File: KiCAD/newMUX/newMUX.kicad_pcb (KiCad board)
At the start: 4 copper layers, 40 x 89 mm, 43 parts, among them J1 Conn_01x14, J2 Conn_02x06_Odd_Even, J3 Conn_02x06_Odd_Even, J4 Conn_01x14, U1 ASSR-1611, U10 ASSR-1611, U11 ASSR-1611, U12 ASSR-1611, U13 ASSR-1611, U14 ASSR-1611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

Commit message: update silk
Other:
- board text added: "c75b306"
- board text removed: "1ad7c5f"
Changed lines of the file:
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@@
   )
   (setup
-    (last_trace_width 1)
+    (last_trace_width 0.25)
     (user_trace_width 0.43)
     (user_trace_width 1)
@@
   (gr_arc (start -17.5 -42) (end -17.5 -44.5) (angle -90) (layer Edge.Cuts) (width 0.15))
   (gr_arc (start 17.5 -42) (end 20 -42) (angle -90) (layer Edge.Cuts) (width 0.15))
-  (gr_text 1ad7c5f (at -18.796 -21.844 90) (layer F.SilkS)
+  (gr_text c75b306 (at -18.796 -21.844 90) (layer F.SilkS)
     (effects (font (size 1 1) (thickness 0.25)))
   )

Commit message: wip commit
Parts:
- RN1, RN2, RN3, RN4, RN5: footprint Resistors_SMD:R_Cat16-4 -> myParts:VISHAY_CRA12E
- moved RN1 0.61 mm to (2.50, 23.0)
- moved RN2 0.61 mm to (-2.50, 23.0)
- moved RN4 0.60 mm to (-2.50, -11.5)
- moved RN5 0.60 mm to (2.50, -11.5)
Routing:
- net Net-(RN1-Pad4): track 22.8 -> 2.97 mm, vias 1 -> 0
- net GND: track 207.1 -> 201.3 mm
- net Net-(RN3-Pad4): track 55.2 -> 59.9 mm, vias 1 -> 2
- net /P7: track 79.7 -> 76.9 mm
- net Net-(RN5-Pad6): track 17.4 -> 20.0 mm
- net Net-(RN5-Pad5): track 43.6 -> 45.7 mm, vias 1 -> 0
- net Net-(RN2-Pad7): track 18.3 -> 20.2 mm, vias 1 -> 2
- net Net-(RN4-Pad2): track 25.6 -> 23.8 mm
- net Net-(R1-Pad2): track 42.6 -> 44.4 mm, vias 3 -> 4
- net Net-(RN2-Pad6): track 10.7 -> 12.3 mm
- net Net-(RN2-Pad5): track 12.2 -> 10.6 mm
- net Net-(RN5-Pad7): track 4.05 -> 2.46 mm, vias 1 -> 0
- net Net-(RN3-Pad1): track 33.3 -> 34.9 mm, vias 1 -> 2
- net Net-(RN5-Pad8): track 12.6 -> 11.1 mm
- net Net-(RN1-Pad3): track 24.4 -> 25.9 mm
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
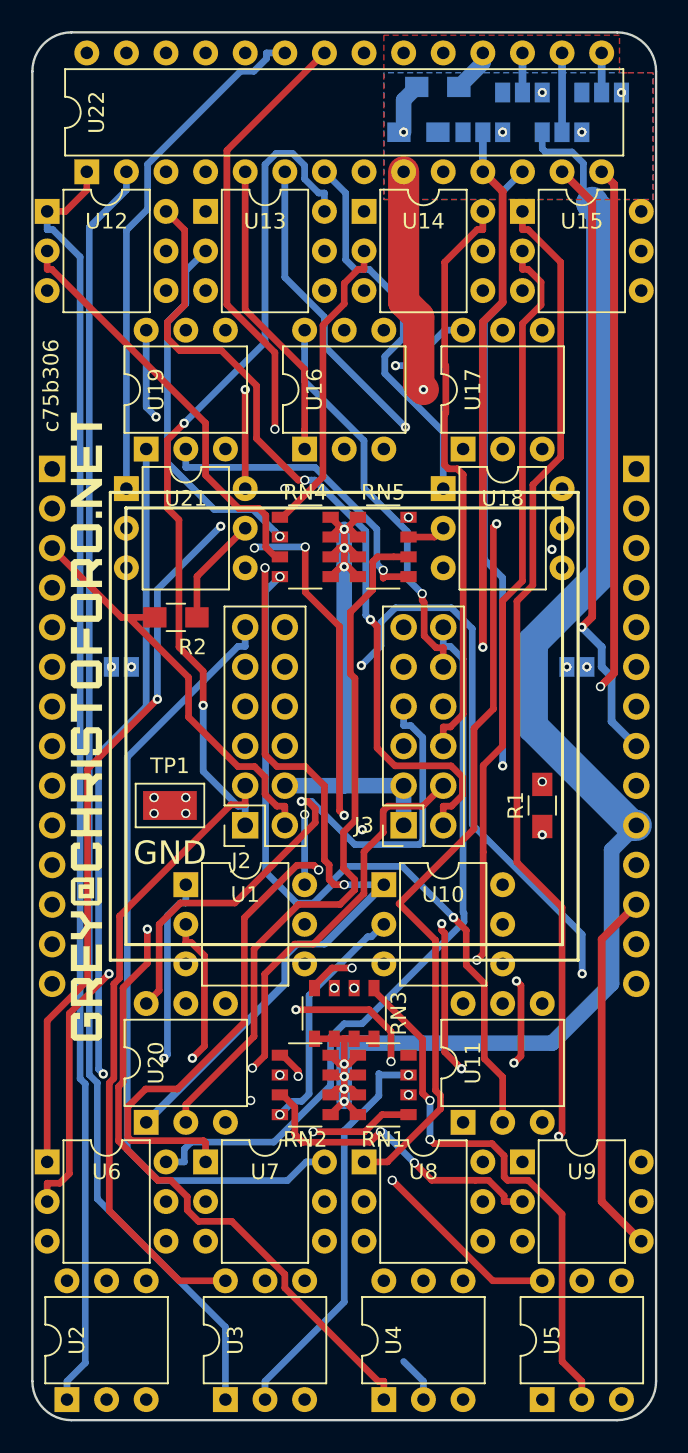
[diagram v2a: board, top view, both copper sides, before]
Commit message: rotate connectors on newMux
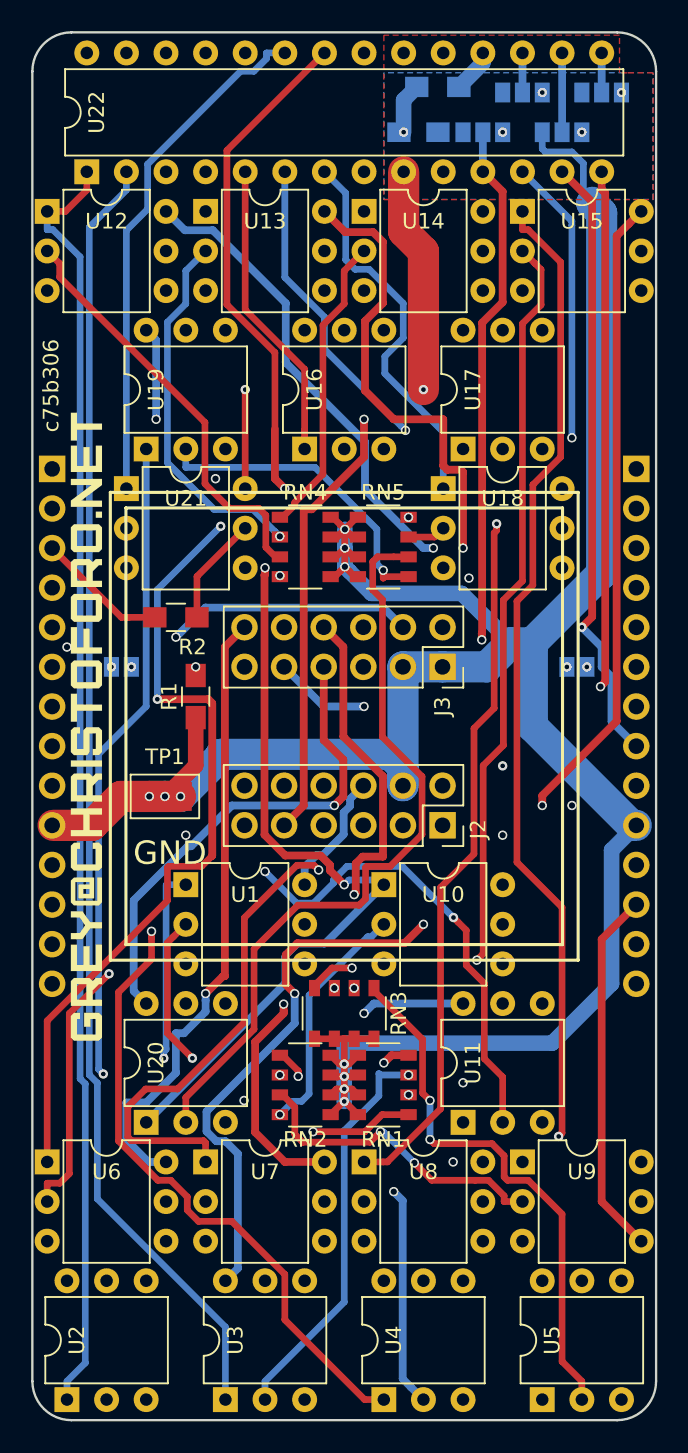
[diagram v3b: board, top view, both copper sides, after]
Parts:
- moved R1 23.3 mm to (-9.53, -1.91)
- moved J2 12.7 mm to (6.30, 6.35), turned to 270 degrees
- moved J3 10.5 mm to (6.30, -3.81), turned to 270 degrees
- moved TP1 0.66 mm to (-11.5, 4.50)
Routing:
- net Net-(R1-Pad2): track 44.4 -> 10.7 mm, vias 4 -> 1
- net /V6: track 50.9 -> 26.7 mm, vias 0 -> 1
- net /I4: track 75.9 -> 52.7 mm, vias 0 -> 1
- net GND: track 201.3 -> 178.2 mm, vias 12 -> 10
- net /I7: track 14.5 -> 36.4 mm, vias 0 -> 1
- net Net-(RN1-Pad4): track 2.97 -> 24.4 mm, vias 0 -> 2
- net /V1: track 45.0 -> 64.4 mm, vias 1 -> 2
- net /I1: track 53.3 -> 35.9 mm, vias 2 -> 1
- net I+: track 151.6 -> 135.0 mm
- net /V8: track 53.7 -> 44.7 mm, vias 2 -> 1
- net /I8: track 23.5 -> 31.8 mm
- net /V4: track 50.7 -> 42.7 mm, vias 3 -> 1
- net /V3: track 43.1 -> 50.5 mm, vias 2 -> 3
- net /I6: track 29.9 -> 37.2 mm
- net /V5: track 47.5 -> 40.3 mm, vias 0 -> 1
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
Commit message: update silk
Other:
- board text added: "3ec2e93"
- board text removed: "c75b306"
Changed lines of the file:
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@@
   )
   (setup
-    (last_trace_width 0.5)
+    (last_trace_width 0.25)
     (user_trace_width 0.43)
     (user_trace_width 0.5)
@@
     )
   )
+  (gr_text 3ec2e93 (at -18.415 -22.225 90) (layer F.SilkS)
+    (effects (font (size 1.5 1.5) (thickness 0.3)))
+  )
   (gr_text "GND\n" (at -11.176 8.128) (layer F.SilkS)
     (effects (font (size 1.5 1.5) (thickness 0.3)))
@@
   (gr_arc (start -17.5 -42) (end -17.5 -44.5) (angle -90) (layer Edge.Cuts) (width 0.15))
   (gr_arc (start 17.5 -42) (end 20 -42) (angle -90) (layer Edge.Cuts) (width 0.15))
-  (gr_text c75b306 (at -18.796 -21.844 90) (layer F.SilkS)
-    (effects (font (size 1 1) (thickness 0.25)))
-  )
   (gr_line (start 20 42) (end 20 -42) (layer Edge.Cuts) (width 0.15))
   (gr_line (start -20 42) (end -20 -42) (layer Edge.Cuts) (width 0.15))

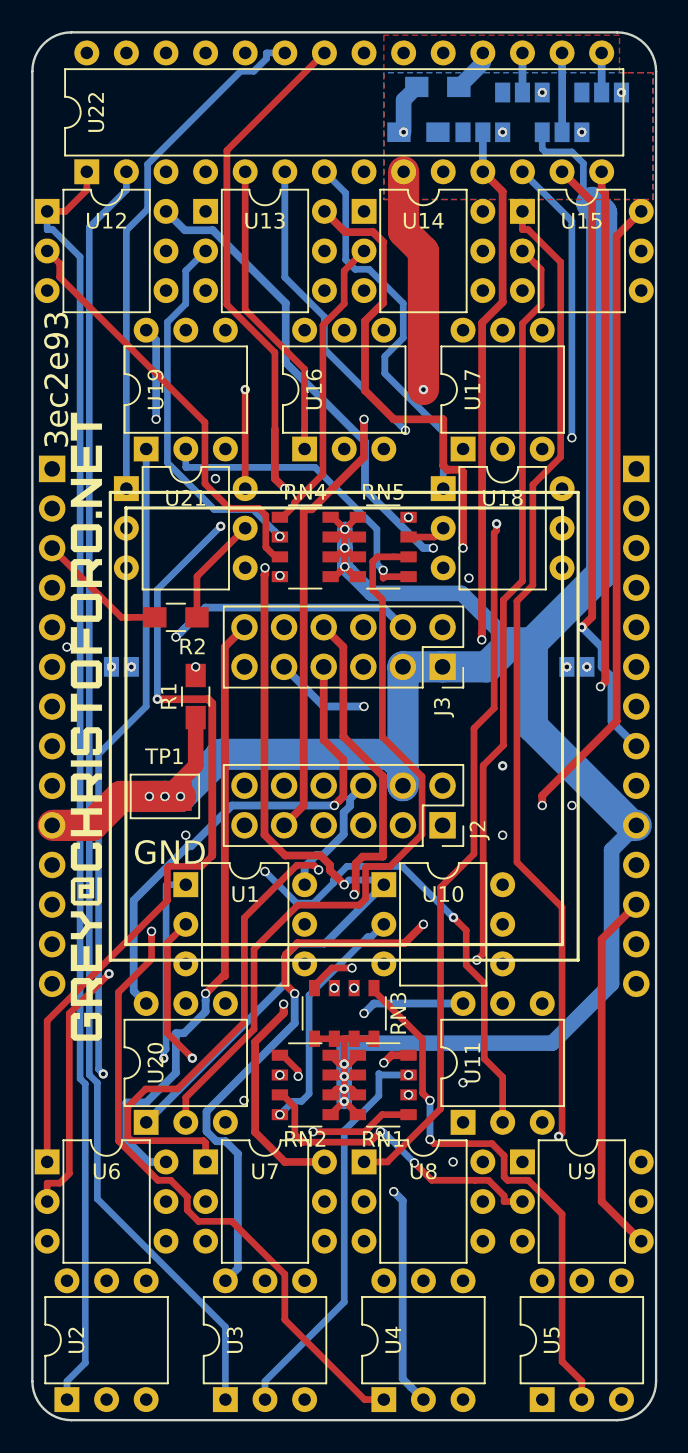
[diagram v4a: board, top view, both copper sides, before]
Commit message: starting on ethercat board pin boards rotated base1x zones fixed
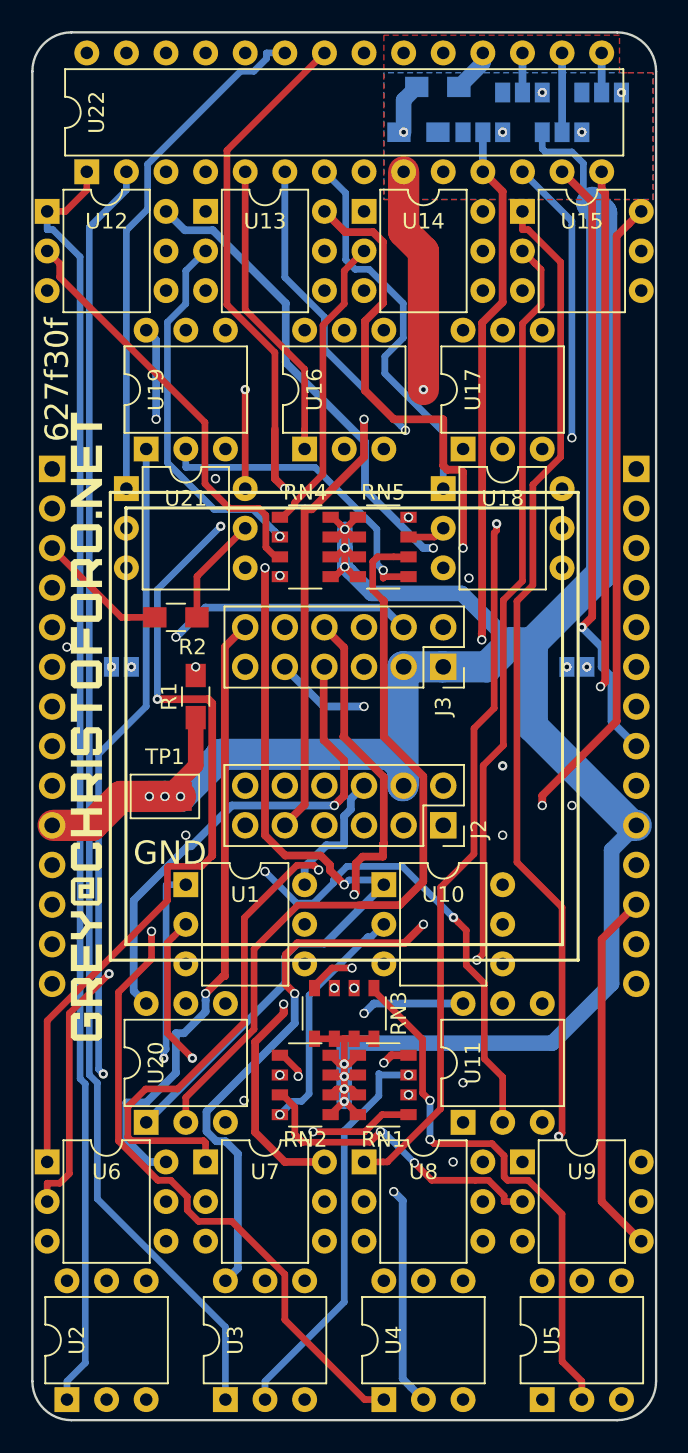
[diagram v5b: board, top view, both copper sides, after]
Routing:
- net Net-(RN5-Pad5): track 49.2 -> 49.9 mm
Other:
- board text added: "627f30f"
- board text removed: "3ec2e93"

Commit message: update silk
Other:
- board text added: "20b2bb8"
- board text removed: "627f30f"
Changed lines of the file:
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@@
-(kicad_pcb (version 20171130) (host pcbnew "(5.0-dev-4085-g9241a399a)")
+(kicad_pcb (version 20171130) (host pcbnew "(5.0.0-rc2-dev-44-gde6b32d23)")
   (general
     (thickness 1.6)
@@
   )
   (setup
-    (last_trace_width 0.5)
+    (last_trace_width 0.25)
     (user_trace_width 0.43)
     (user_trace_width 0.5)
@@
       (usegerberattributes true)
       (usegerberadvancedattributes true)
-      (creategerberjobfile true)
+      (creategerberjobfile false)
       (excludeedgelayer true)
       (linewidth 0.150000)
@@
     )
   )
-  (gr_text 627f30f (at -18.415 -22.225 90) (layer F.SilkS)
+  (gr_text 20b2bb8 (at -18.415 -22.225 90) (layer F.SilkS)
     (effects (font (size 1.5 1.5) (thickness 0.3)))
   )

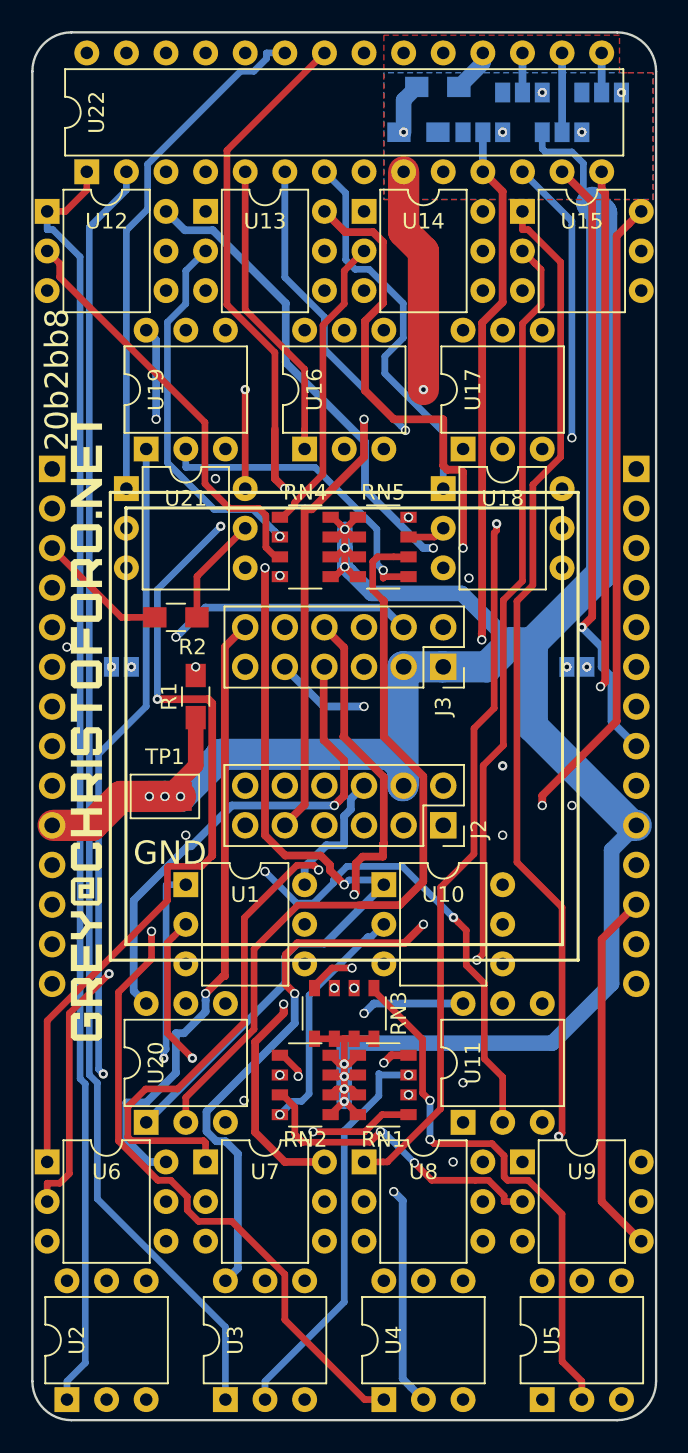
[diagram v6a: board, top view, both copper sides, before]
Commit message: upgrade syms and layouts to kicad5
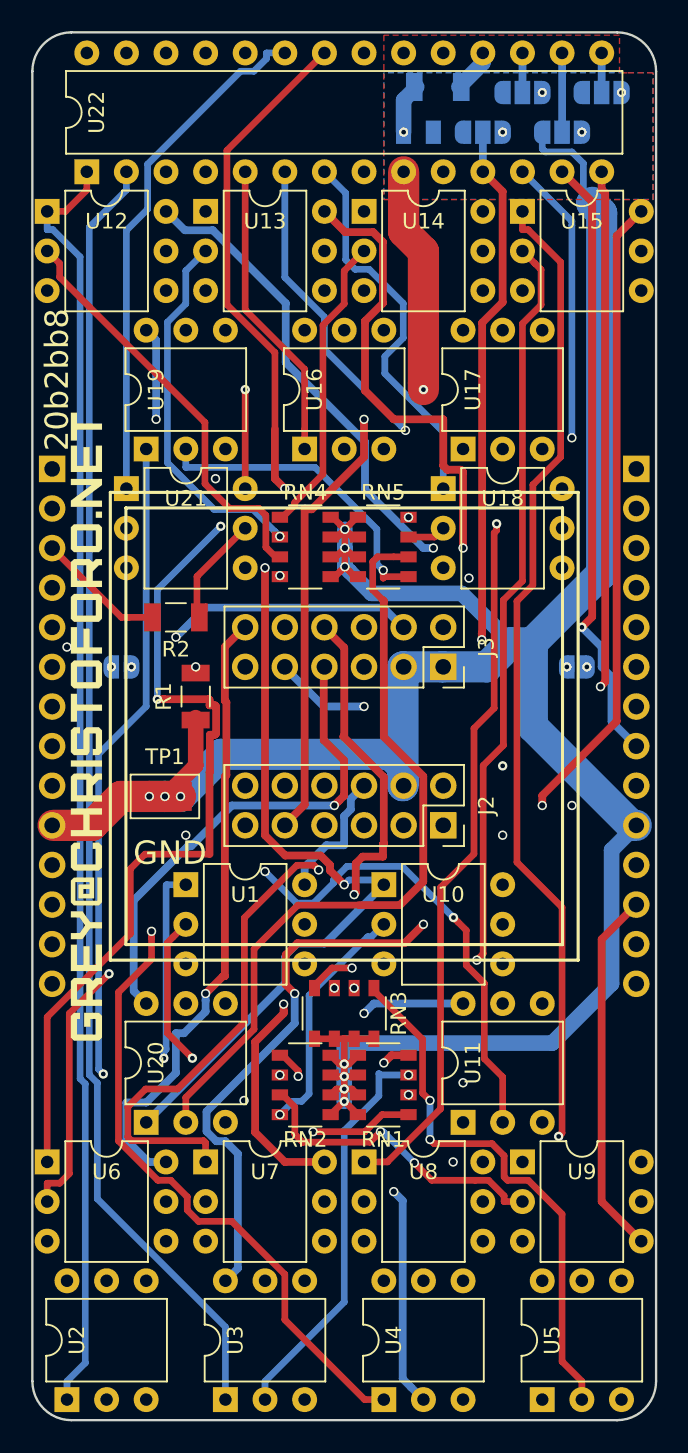
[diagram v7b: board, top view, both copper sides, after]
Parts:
- C1: footprint Capacitors_SMD:C_0805_HandSoldering -> Capacitor_SMD:C_0805_2012Metric
- J1, J4: footprint Pin_Headers:Pin_Header_Straight_1x14_Pitch2.54mm -> Connector_PinHeader_2.54mm:PinHeader_1x14_P2.54mm_Vertical
- J2, J3: footprint Socket_Strips:Socket_Strip_Straight_2x06_Pitch2.54mm -> Connector_PinSocket_2.54mm:PinSocket_2x06_P2.54mm_Vertical
- JP1, JP6: footprint Connect:GS2 -> Jumper:SolderJumper-2_P1.3mm_Open_RoundedPad1.0x1.5mm
- JP2, JP3, JP4, JP5: footprint Connect:GS3 -> Jumper:SolderJumper-3_P1.3mm_Open_RoundedPad1.0x1.5mm_NumberLabels
- R1, R2, R3: footprint Resistors_SMD:R_0805_HandSoldering -> Resistor_SMD:R_1206_3216Metric
- U1, U10, U11, U12, U13, U14, U15, U16, U17, U18, U19, U2, U20, U21, U3, U4, U5, U6, U7, U8, U9: footprint Housings_DIP:DIP-6_W7.62mm -> Package_DIP:DIP-6_W7.62mm
- U22: footprint Housings_DIP:DIP-28_W7.62mm -> Package_DIP:DIP-28_W7.62mm
- turned JP1 to 180 degrees
- turned JP2 to 180 degrees
- turned JP3 to 180 degrees
- turned JP4 to 180 degrees
- turned JP5 to 180 degrees
- turned JP6 to 180 degrees
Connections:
- U1 pad 3: (no net) -> Net-(U1-Pad3)
- U1 pad 5: (no net) -> Net-(U1-Pad5)
- U10 pad 3: (no net) -> Net-(U10-Pad3)
- U10 pad 5: (no net) -> Net-(U10-Pad5)
- U11 pad 3: (no net) -> Net-(U11-Pad3)
- U11 pad 5: (no net) -> Net-(U11-Pad5)
- U12 pad 3: (no net) -> Net-(U12-Pad3)
- U12 pad 5: (no net) -> Net-(U12-Pad5)
- U13 pad 3: (no net) -> Net-(U13-Pad3)
- U13 pad 5: (no net) -> Net-(U13-Pad5)
- U14 pad 3: (no net) -> Net-(U14-Pad3)
- U14 pad 5: (no net) -> Net-(U14-Pad5)
- U15 pad 3: (no net) -> Net-(U15-Pad3)
- U15 pad 5: (no net) -> Net-(U15-Pad5)
- U16 pad 3: (no net) -> Net-(U16-Pad3)
- U16 pad 5: (no net) -> Net-(U16-Pad5)
- U17 pad 3: (no net) -> Net-(U17-Pad3)
- U17 pad 5: (no net) -> Net-(U17-Pad5)
- U18 pad 3: (no net) -> Net-(U18-Pad3)
- U18 pad 5: (no net) -> Net-(U18-Pad5)
- U19 pad 3: (no net) -> Net-(U19-Pad3)
- U19 pad 5: (no net) -> Net-(U19-Pad5)
- U2 pad 3: (no net) -> Net-(U2-Pad3)
- U2 pad 5: (no net) -> Net-(U2-Pad5)
- U20 pad 3: (no net) -> Net-(U20-Pad3)
- U20 pad 5: (no net) -> Net-(U20-Pad5)
- U21 pad 3: (no net) -> Net-(U21-Pad3)
- U21 pad 4: (no net) -> Net-(U21-Pad4)
- U22 pad 19: (no net) -> Net-(U22-Pad19)
- U22 pad 20: (no net) -> Net-(U22-Pad20)
- U22 pad 24: (no net) -> Net-(U22-Pad24)
- U22 pad 25: (no net) -> Net-(U22-Pad25)
- U22 pad 26: (no net) -> Net-(U22-Pad26)
- U22 pad 27: (no net) -> Net-(U22-Pad27)
- U22 pad 28: (no net) -> Net-(U22-Pad28)
- U3 pad 3: (no net) -> Net-(U3-Pad3)
- U3 pad 5: (no net) -> Net-(U3-Pad5)
- U4 pad 3: (no net) -> Net-(U4-Pad3)
- U4 pad 5: (no net) -> Net-(U4-Pad5)
- U5 pad 3: (no net) -> Net-(U5-Pad3)
- U5 pad 5: (no net) -> Net-(U5-Pad5)
- U6 pad 3: (no net) -> Net-(U6-Pad3)
- U6 pad 5: (no net) -> Net-(U6-Pad5)
- U7 pad 3: (no net) -> Net-(U7-Pad3)
- U7 pad 5: (no net) -> Net-(U7-Pad5)
- U8 pad 3: (no net) -> Net-(U8-Pad3)
- U8 pad 5: (no net) -> Net-(U8-Pad5)
- U9 pad 3: (no net) -> Net-(U9-Pad3)
- U9 pad 5: (no net) -> Net-(U9-Pad5)
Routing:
- net /P5: track 79.2 -> 81.0 mm

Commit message: update silk before order 629bf0f
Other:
- board text added: "629bf0f"
- board text removed: "20b2bb8"
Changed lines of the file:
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@@
   )
   (setup
-    (last_trace_width 0.43)
+    (last_trace_width 0.25)
     (user_trace_width 0.43)
     (user_trace_width 0.5)
@@
     )
   )
-  (gr_text 20b2bb8 (at -18.415 -22.225 90) (layer F.SilkS)
+  (gr_text 629bf0f (at -18.415 -22.225 90) (layer F.SilkS)
     (effects (font (size 1.5 1.5) (thickness 0.3)))
   )
